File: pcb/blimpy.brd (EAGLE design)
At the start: 250 x 167 mm, 72 parts, among them J1 MICRO-USB, J4 3-PIN SMD, J5 3-PIN SMD, J6 3-PIN SMD, J7 3-PIN SMD, Q1 mmbt2222, Q2 mmbt2222, Q3 DMG3415U, U1 RGB, U10 MAX17048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

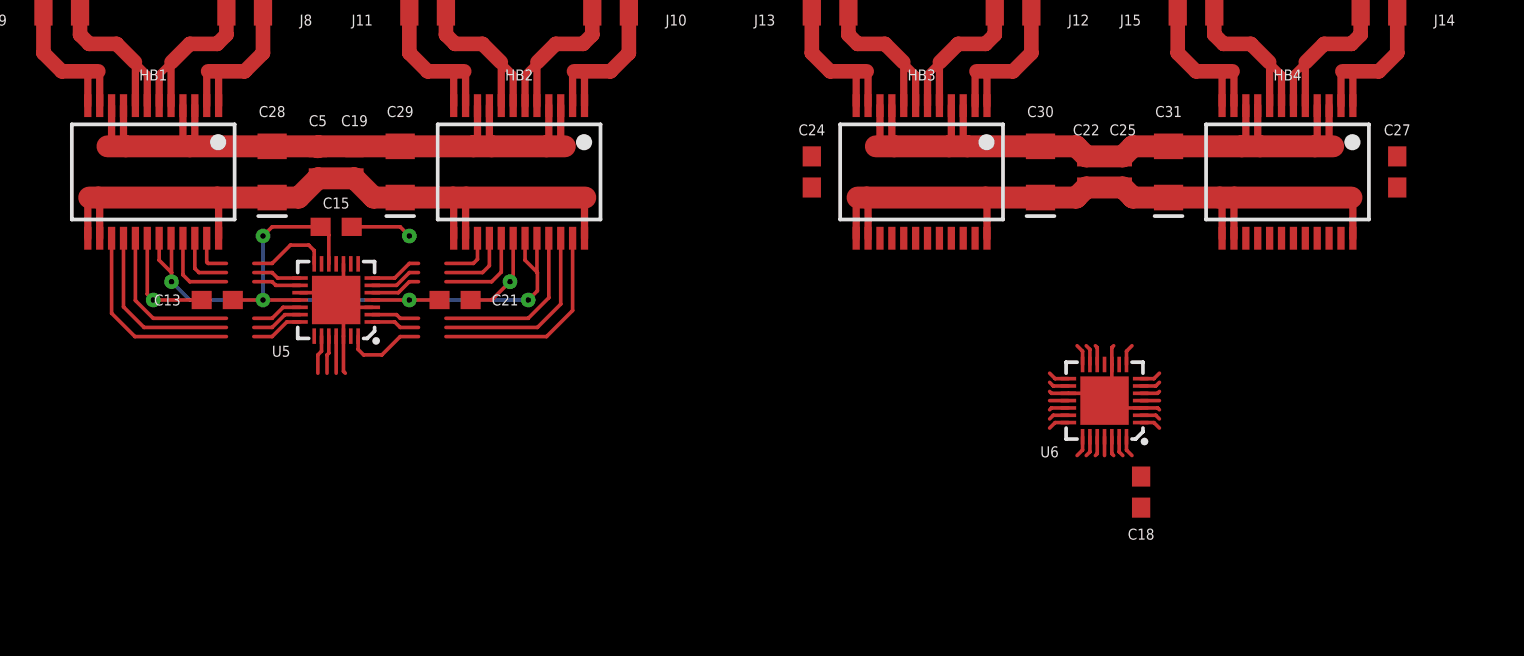
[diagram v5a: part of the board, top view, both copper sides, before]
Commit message: finished hbridge io
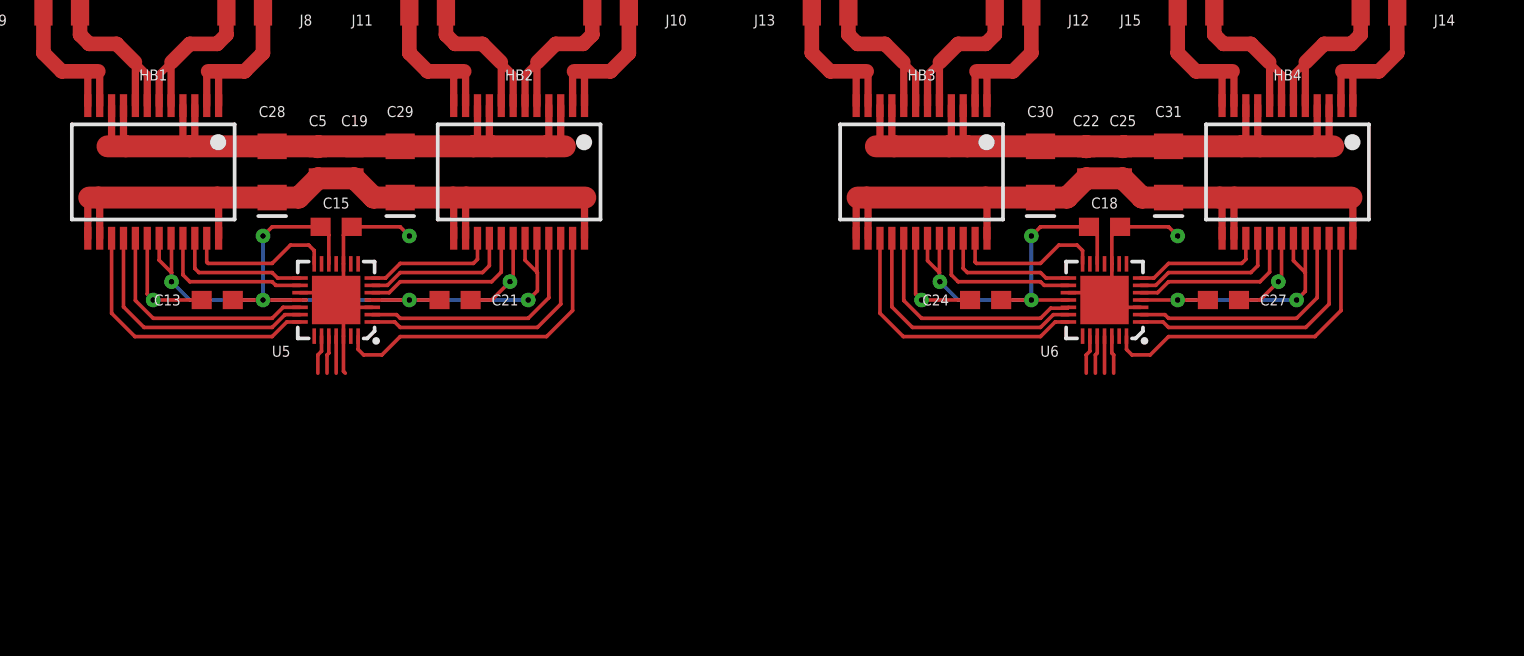
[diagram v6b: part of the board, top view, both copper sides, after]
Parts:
- moved C18 14.6 mm to (93.5, 140.5), turned to 0 degrees
- moved C24 11.8 mm to (87.0, 136.5), turned to 180 degrees
- moved C27 11.8 mm to (100.0, 136.5), turned to 0 degrees
- moved U6 5.50 mm to (93.5, 136.5)
- moved C22 0.50 mm to (92.5, 144.0)
- moved C25 0.50 mm to (94.5, 144.0)
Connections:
- removed net 1-1: U5.27
- removed net 1-10: U5.14
- removed net 1-11: U5.15
- removed net 1-12: U5.16
- removed net 1-13: U5.19
- removed net 1-14: U5.20
- removed net 1-15: U5.21
- removed net 1-16: U5.22
- removed net 1-2: U5.28
- removed net 1-3: U5.1
- removed net 1-4: U5.2
- removed net 1-5: U5.5
- removed net 1-6: U5.6
- removed net 1-7: U5.7
- removed net 1-8: U5.8
- removed net 1-9: U5.13
- removed net 2-1: U6.27
- removed net 2-10: U6.14
- removed net 2-11: U6.15
- removed net 2-12: U6.16
- removed net 2-13: U6.19
- removed net 2-14: U6.20
- removed net 2-15: U6.21
- removed net 2-16: U6.22
- removed net 2-2: U6.28
- removed net 2-3: U6.1
- removed net 2-4: U6.2
- removed net 2-5: U6.5
- removed net 2-6: U6.6
- removed net 2-7: U6.7
- removed net 2-8: U6.8
- removed net 2-9: U6.13
- removed net H1-1: HB1.23
- removed net H1-2: HB1.22
- removed net H1-3: HB1.21
- removed net H1-4: HB1.17
- removed net H1-5: HB1.16
- removed net H1-6: HB1.15
- removed net H2-1: HB2.23
- removed net H2-2: HB2.22
- removed net H2-3: HB2.21
- removed net H2-4: HB2.17
- removed net H2-5: HB2.16
- removed net H2-6: HB2.15
- removed net H3-1: HB3.23
- removed net H3-2: HB3.22
- removed net H3-3: HB3.21
- removed net H3-4: HB3.17
- removed net H3-5: HB3.16
- removed net H3-6: HB3.15
- removed net H4-1: HB4.23
- removed net H4-2: HB4.22
- removed net H4-3: HB4.21
- removed net H4-4: HB4.17
- removed net H4-5: HB4.16
- removed net H4-6: HB4.15
- new net H1-AIN1: HB1.21, U5.16
- new net H1-AIN2: HB1.22, U5.15
- new net H1-APWM: HB1.23, U5.14
- new net H1-BIN1: HB1.17, U5.19
- new net H1-BIN2: HB1.16, U5.20
- new net H1-BPWM: HB1.15, U5.21
- new net H2-AIN1: HB2.21, U5.2
- new net H2-AIN2: HB2.22, U5.1
- new net H2-APWM: HB2.23, U5.28
- new net H2-BIN1: HB2.17, U5.5
- new net H2-BIN2: HB2.16, U5.6
- new net H2-BPWM: HB2.15, U5.7
- new net H3-AIN1: HB3.21, U6.16
- new net H3-AIN2: HB3.22, U6.15
- new net H3-APWM: HB3.23, U6.14
- new net H3-BIN1: HB3.17, U6.19
- new net H3-BIN2: HB3.16, U6.20
- new net H3-BPWM: HB3.15, U6.21
- new net H4-AIN1: HB4.21, U6.2
- new net H4-AIN2: HB4.22, U6.1
- new net H4-APWM: HB4.23, U6.28
- new net H4-BIN1: HB4.17, U6.5
- new net H4-BIN2: HB4.16, U6.6
- new net H4-BPWM: HB4.15, U6.7
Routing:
- net 3.3V: track 50.8 -> 87.2 mm, vias 5 -> 10
- net H4-APWM: track 0.00 -> 17.5 mm
- net H2-APWM: track 0.00 -> 17.5 mm
- net GND: track 121.5 -> 136.9 mm, vias 3 -> 6
- net H3-BPWM: track 0.00 -> 15.3 mm
- net H1-BPWM: track 0.00 -> 15.3 mm
- net H4-AIN2: track 0.00 -> 14.6 mm
- net H2-AIN2: track 0.00 -> 14.6 mm
- net H3-BIN2: track 0.00 -> 14.2 mm
- net H1-BIN2: track 0.00 -> 14.2 mm
- net H4-AIN1: track 0.00 -> 13.4 mm
- net H2-AIN1: track 0.00 -> 13.4 mm
- net H3-BIN1: track 0.00 -> 13.1 mm
- net H1-BIN1: track 0.00 -> 13.1 mm
- net H2-1: track 11.5 -> 0.00 mm
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
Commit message: move on place
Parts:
- moved J7 186.1 mm to (51.0, 7.00), turned to 180 degrees
- moved J14 179.6 mm to (9.00, 8.00), turned to 180 degrees
- moved J6 173.2 mm to (63.0, 7.00), turned to 180 degrees
- moved J15 169.3 mm to (19.0, 8.00), turned to 180 degrees
- moved J12 160.9 mm to (29.0, 8.00), turned to 180 degrees
- moved J13 154.6 mm to (39.0, 8.00), turned to 180 degrees
- moved HB4 150.9 mm to (14.0, 22.0), turned to 0 degrees
- moved C31 143.6 mm to (20.5, 22.0), turned to 90 degrees
- moved C25 141.8 mm to (23.0, 21.5), turned to 270 degrees
- moved C22 139.9 mm to (25.0, 21.5), turned to 270 degrees
- moved C30 136.6 mm to (27.5, 22.0), turned to 90 degrees
- moved C27 135.5 mm to (17.5, 29.0), turned to 180 degrees
- moved C18 134.8 mm to (24.0, 25.0), turned to 180 degrees
- moved HB3 131.2 mm to (34.0, 22.0), turned to 0 degrees
- moved U6 128.0 mm to (24.0, 29.0), turned to 0 degrees
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
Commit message: small connections
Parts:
- moved R13 124.3 mm to (107.0, 74.0)
- moved R5 123.1 mm to (104.5, 70.0)
- moved R6 122.6 mm to (103.0, 70.0)
- moved U1 122.5 mm to (103.0, 66.5), turned to 0 degrees
- moved R7 122.1 mm to (101.5, 70.0)
- moved R14 121.8 mm to (111.5, 74.0), turned to 90 degrees
- moved R11 121.6 mm to (111.0, 99.0)
- moved U9 121.6 mm to (105.9, 86.8)
- moved R16 9.62 mm to (58.0, 69.5), turned to 90 degrees
- moved R8 8.73 mm to (59.0, 58.0), turned to 270 degrees
- moved R15 8.14 mm to (56.5, 58.0), turned to 270 degrees
- moved C2 3.54 mm to (16.0, 76.5)
- moved U7 3.00 mm to (19.0, 81.0)
- moved C11 1.12 mm to (50.5, 76.0), turned to 90 degrees
- moved R9 0.50 mm to (33.5, 88.0)
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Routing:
- net N$6: track 0.00 -> 5.32 mm, vias 0 -> 2
- net 3.3V: track 87.2 -> 92.2 mm
- net N$10: track 0.00 -> 4.33 mm
- net N$2: track 0.00 -> 3.45 mm
- net N$9: track 0.00 -> 2.41 mm
- net N$11: track 0.00 -> 2.41 mm
- net CHIP_EN: track 0.00 -> 2.41 mm
- net RTS: track 0.00 -> 1.61 mm
- net N$13: track 0.00 -> 1.61 mm
- net N$12: track 0.00 -> 1.61 mm
- net DTR: track 0.00 -> 1.61 mm
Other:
- board size 250 x 167 mm -> 135 x 167 mm
